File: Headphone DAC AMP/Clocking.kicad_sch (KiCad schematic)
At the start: 9 parts, among them Y1 LMK6CE049152CDLFR, Y2 LMK6CE049152CDLFR, Y3 ASDLJ-E-45.1584MHz

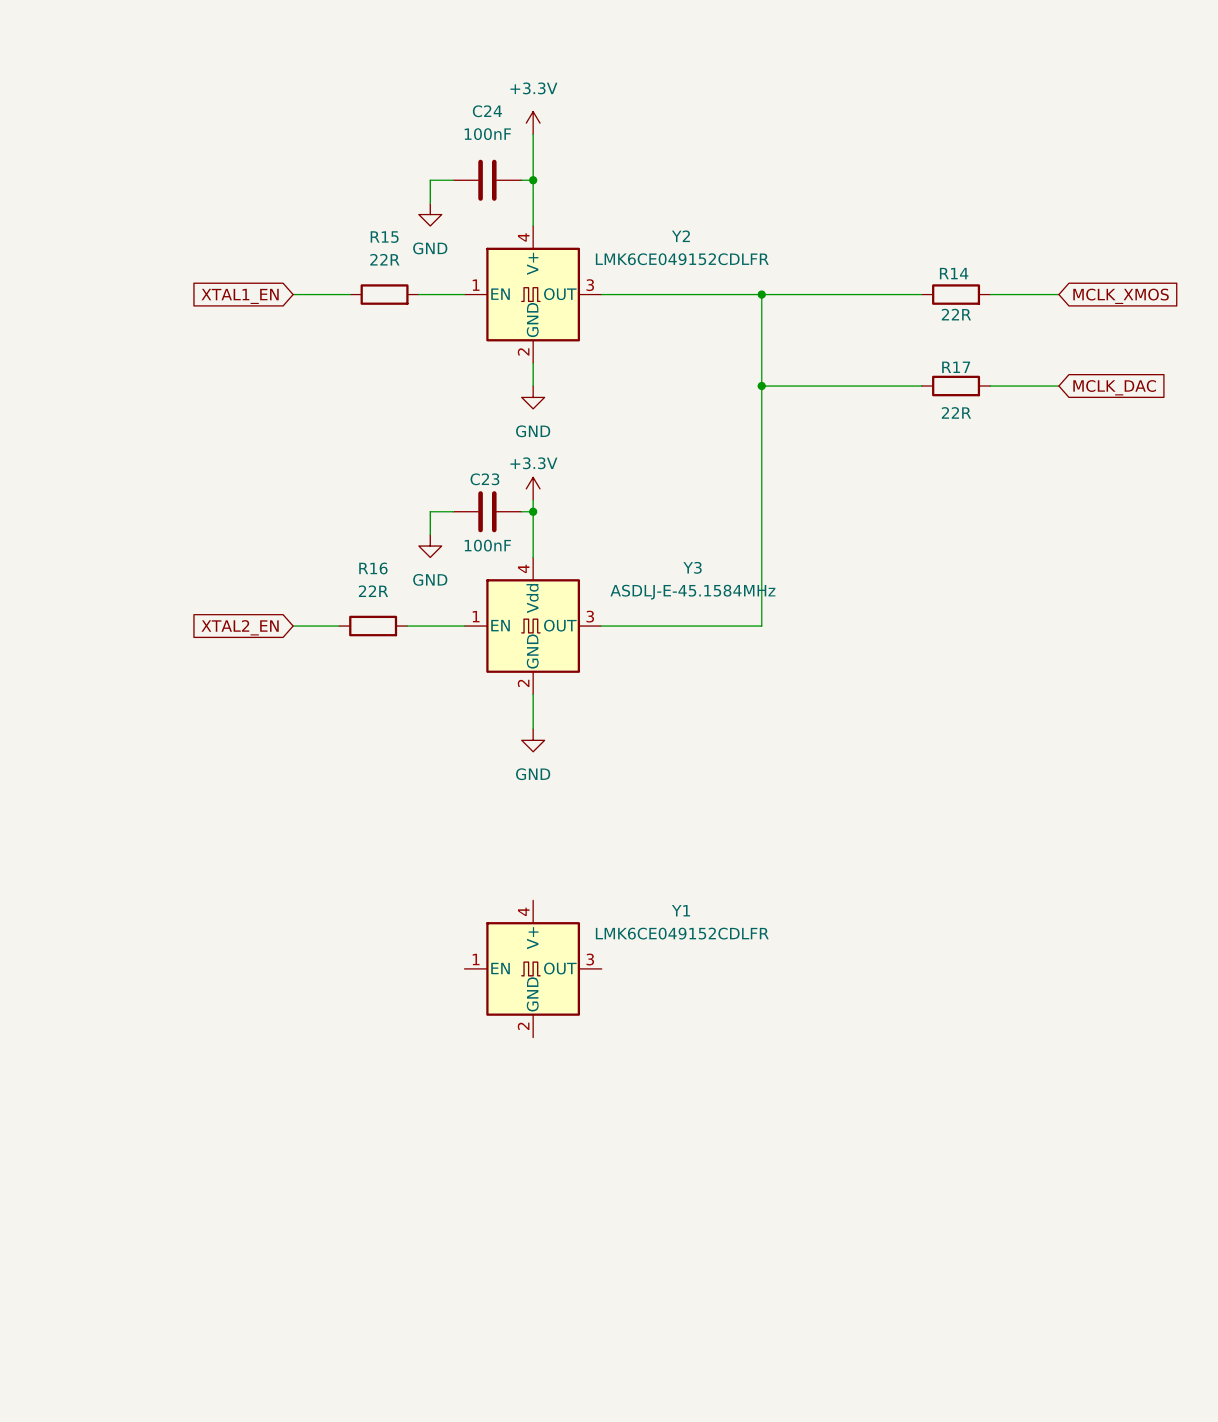
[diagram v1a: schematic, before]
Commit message: Completed a significant amount of the power and routing
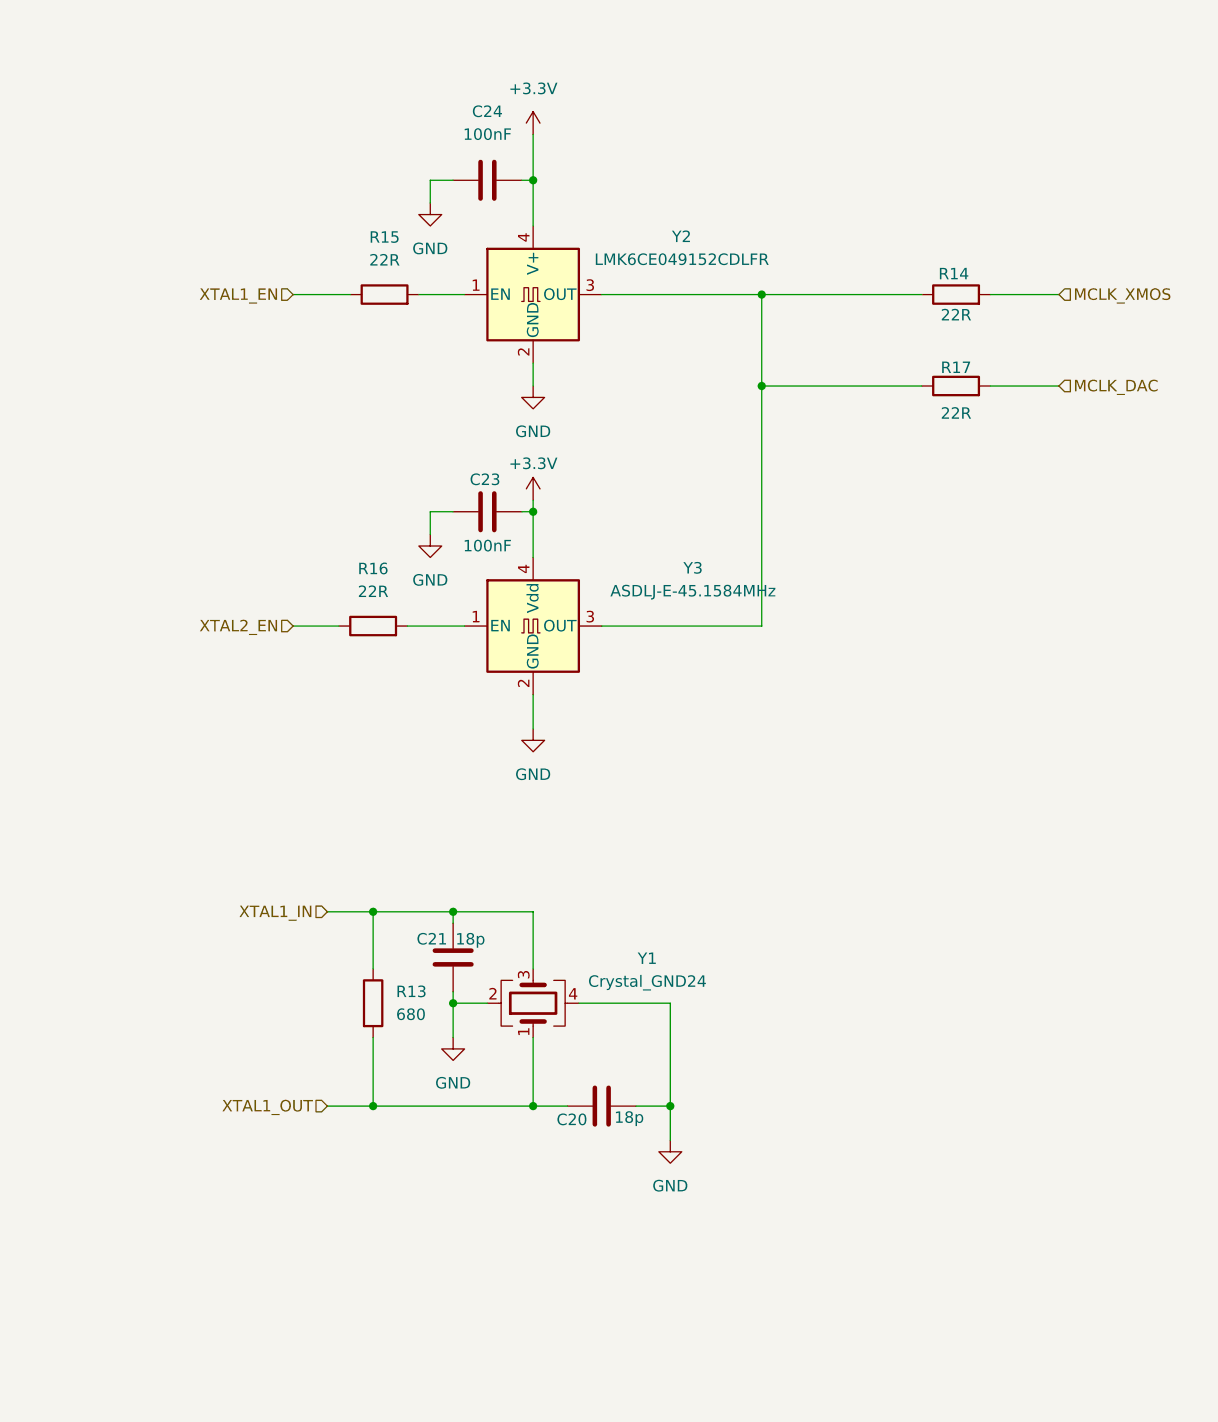
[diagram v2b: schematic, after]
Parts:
- removed Y1: LMK6CE049152CDLFR, Oscillator:Oscillator_SMD_EuroQuartz_XO32-4Pin_3.2x2.5mm, symbol Oscillator:XO32
- added C20, C21: 18p, Capacitor_SMD:C_0805_2012Metric_Pad1.18x1.45mm_HandSolder, symbol Device:C
- added R13: 680, Resistor_SMD:R_0805_2012Metric_Pad1.20x1.40mm_HandSolder, symbol Device:R
- added Y1: Crystal_GND24, Crystal:Crystal_SMD_3225-4Pin_3.2x2.5mm_HandSoldering, symbol Device:Crystal_GND24
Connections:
- net GND: now also C20.1, C21.2, Y1.2, Y1.4
- new net XTAL1_IN: C21.1, R13.1, Y1.3
- new net XTAL1_OUT: C20.2, R13.2, Y1.1

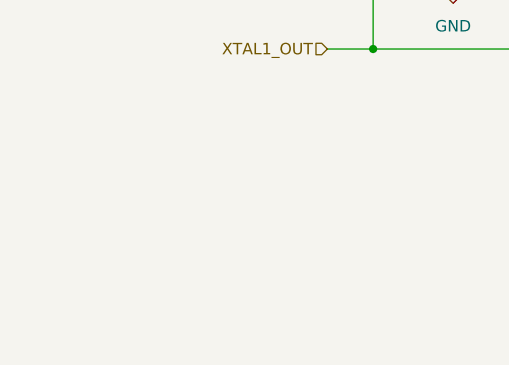
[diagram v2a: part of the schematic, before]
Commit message: Added ground and 0.9v
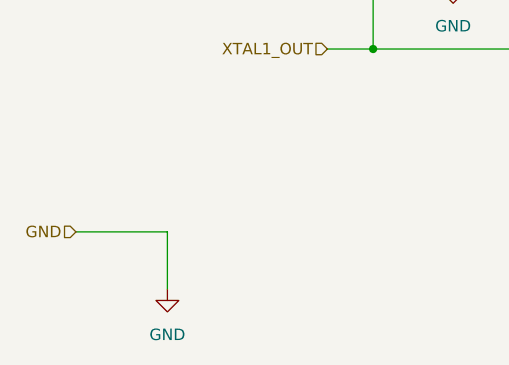
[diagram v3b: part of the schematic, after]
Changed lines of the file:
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@@
+	(wire
+		(pts
+			(xy 46.99 158.75) (xy 57.15 158.75)
+		)
+		(stroke
+			(width 0)
+			(type default)
+		)
+	)
 	(wire
 		(pts
@@
 		(pts
 			(xy 123.19 58.42) (xy 140.97 58.42)
+		)
+		(stroke
+			(width 0)
+			(type default)
+		)
+	)
+	(wire
+		(pts
+			(xy 57.15 158.75) (xy 57.15 165.1)
 		)
 		(stroke
@@
 			)
 			(justify left)
+		)
+	)
+	(hierarchical_label "GND"
+		(shape input)
+		(at 46.99 158.75 180)
+		(effects
+			(font
+				(size 1.27 1.27)
+			)
+			(justify right)
 		)
 	)
@@
 					(unit 1)
 				)
+			)
+		)
+	)
+	(symbol
+		(lib_id "power:GND")
+		(at 57.15 165.1 0)
+		(unit 1)
+		(exclude_from_sim no)
+		(in_bom yes)
+		(on_board yes)
+		(dnp no)
+		(fields_autoplaced yes)
+		(property "Reference" "#PWR083"
+			(at 57.15 171.45 0)
+			(effects
+				(font
+					(size 1.27 1.27)
+				)
+				(hide yes)
+			)
+		)
+		(property "Value" "GND"
+			(at 57.15 170.18 0)
+			(effects
+				(font
+					(size 1.27 1.27)
+				)
+			)
+		)
+		(property "Footprint" ""
+			(at 57.15 165.1 0)
+			(effects
+				(font
+					(size 1.27 1.27)
+				)
+				(hide yes)
+			)
+		)
+		(property "Datasheet" ""
+			(at 57.15 165.1 0)
+			(effects
+				(font
+					(size 1.27 1.27)
+				)
+				(hide yes)
+			)
+		)
+		(property "Description" "Power symbol creates a global label with name \"GND\" , ground"
+			(at 57.15 165.1 0)
+			(effects
+				(font
+					(size 1.27 1.27)
+				)
+				(hide yes)
+			)
+		)
+		(pin "1"
+		)
+		(instances
+			(project "Headphone DAC AMP"
+				(path "/d034eddd-efbc-47be-a25c-37cbfbab4cd8/e0b8fe34-d476-48aa-82d1-b0ba2e6c9788"
+					(reference "#PWR083")
+					(unit 1)
+				)

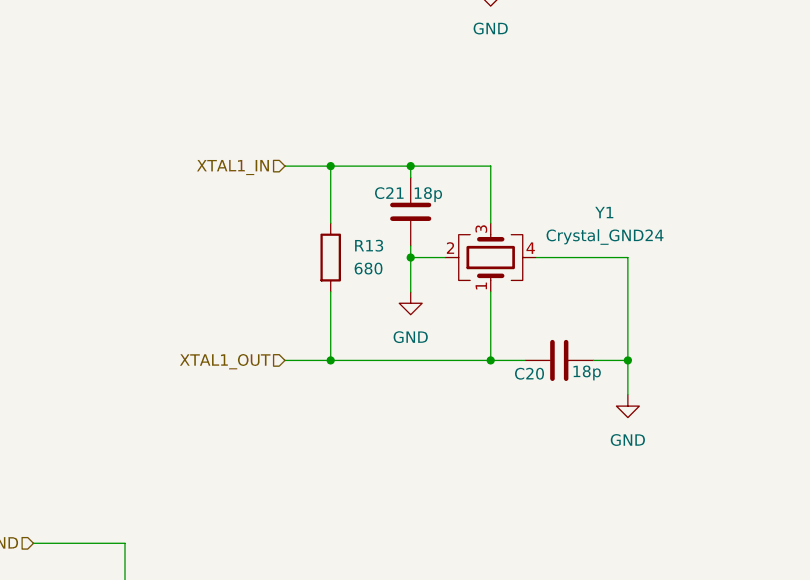
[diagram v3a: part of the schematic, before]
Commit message: fixed 24MHz clock and send draft 1 to tait
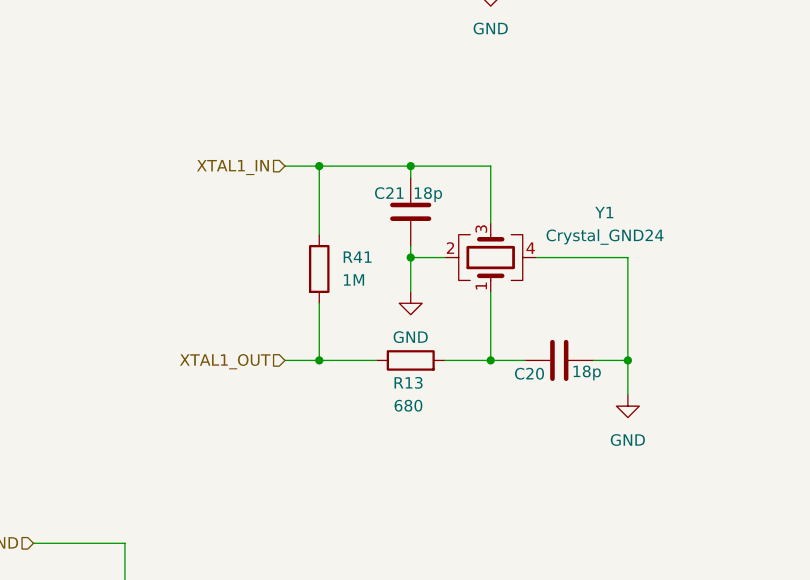
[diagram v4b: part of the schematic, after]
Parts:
- added R41: 1M, symbol Device:R
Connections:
- net XTAL1_IN: now also R41.1; no longer R13.1
- net XTAL1_OUT: now also R13.1, R41.2; no longer C20.2, R13.2, Y1.1
- new net: C20.2, R13.2, Y1.1
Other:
- moved on the sheet: R13
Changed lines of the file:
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@@
+	)
+	(junction
+		(at 97.79 138.43)
+		(diameter 0)
+		(color 0 0 0 0)
 	)
 	(junction
@@
 	)
 	(junction
-		(at 80.01 116.84)
-		(diameter 0)
-		(color 0 0 0 0)
-	)
-	(junction
-		(at 97.79 138.43)
+		(at 78.74 116.84)
 		(diameter 0)
 		(color 0 0 0 0)
@@
 	)
 	(junction
+		(at 78.74 138.43)
+		(diameter 0)
+		(color 0 0 0 0)
+	)
+	(junction
 		(at 97.79 72.39)
 		(diameter 0)
 		(color 0 0 0 0)
 	)
-	(junction
-		(at 80.01 138.43)
-		(diameter 0)
-		(color 0 0 0 0)
-	)
 	(wire
 		(pts
@@
 	(wire
 		(pts
-			(xy 74.93 116.84) (xy 80.01 116.84)
-		)
-		(stroke
-			(width 0)
-			(type default)
-		)
-	)
-	(wire
-		(pts
 			(xy 97.79 30.48) (xy 97.79 35.56)
 		)
@@
 	(wire
 		(pts
+			(xy 78.74 132.08) (xy 78.74 138.43)
+		)
+		(stroke
+			(width 0)
+			(type default)
+		)
+	)
+	(wire
+		(pts
+			(xy 78.74 116.84) (xy 88.9 116.84)
+		)
+		(stroke
+			(width 0)
+			(type default)
+		)
+	)
+	(wire
+		(pts
 			(xy 113.03 138.43) (xy 113.03 142.24)
 		)
@@
 	(wire
 		(pts
-			(xy 80.01 130.81) (xy 80.01 138.43)
-		)
-		(stroke
-			(width 0)
-			(type default)
-		)
-	)
-	(wire
-		(pts
 			(xy 88.9 116.84) (xy 97.79 116.84)
 		)
@@
 	(wire
 		(pts
-			(xy 80.01 116.84) (xy 80.01 123.19)
-		)
-		(stroke
-			(width 0)
-			(type default)
-		)
-	)
-	(wire
-		(pts
 			(xy 123.19 48.26) (xy 140.97 48.26)
 		)
@@
 	(wire
 		(pts
+			(xy 74.93 138.43) (xy 78.74 138.43)
+		)
+		(stroke
+			(width 0)
+			(type default)
+		)
+	)
+	(wire
+		(pts
 			(xy 105.41 85.09) (xy 123.19 85.09)
 		)
@@
 	(wire
 		(pts
-			(xy 101.6 138.43) (xy 97.79 138.43)
-		)
-		(stroke
-			(width 0)
-			(type default)
-		)
-	)
-	(wire
-		(pts
 			(xy 71.12 85.09) (xy 76.2 85.09)
 		)
@@
 	(wire
 		(pts
-			(xy 80.01 116.84) (xy 88.9 116.84)
+			(xy 74.93 116.84) (xy 78.74 116.84)
+		)
+		(stroke
+			(width 0)
+			(type default)
+		)
+	)
+	(wire
+		(pts
+			(xy 78.74 116.84) (xy 78.74 124.46)
 		)
 		(stroke
@@
 	(wire
 		(pts
-			(xy 80.01 138.43) (xy 74.93 138.43)
-		)
-		(stroke
-			(width 0)
-			(type default)
-		)
-	)
-	(wire
-		(pts
 			(xy 148.59 58.42) (xy 156.21 58.42)
 		)
@@
 	(wire
 		(pts
-			(xy 80.01 138.43) (xy 97.79 138.43)
+			(xy 78.74 138.43) (xy 85.09 138.43)
 		)
 		(stroke
@@
 	(wire
 		(pts
+			(xy 92.71 138.43) (xy 97.79 138.43)
+		)
+		(stroke
+			(width 0)
+			(type default)
+		)
+	)
+	(wire
+		(pts
 			(xy 97.79 71.12) (xy 97.79 72.39)
+		)
+		(stroke
+			(width 0)
+			(type default)
+		)
+	)
+	(wire
+		(pts
+			(xy 97.79 138.43) (xy 101.6 138.43)
 		)
 		(stroke
@@
 	(symbol
 		(lib_id "Device:R")
-		(at 80.01 127 0)
-		(unit 1)
-		(exclude_from_sim no)
-		(in_bom yes)
-		(on_board yes)
-		(dnp no)
-		(fields_autoplaced yes)
+		(at 88.9 138.43 90)
+		(unit 1)
+		(exclude_from_sim no)
+		(in_bom yes)
+		(on_board yes)
+		(dnp no)
 		(property "Reference" "R13"
-			(at 82.55 125.7299 0)
-			(effects
-				(font
-					(size 1.27 1.27)
-				)
-				(justify left)
+			(at 88.646 140.97 90)
+			(effects
+				(font
+					(size 1.27 1.27)
+				)
 			)
 		)
 		(property "Value" "680"
-			(at 82.55 128.2699 0)
-			(effects
-				(font
-					(size 1.27 1.27)
-				)
-				(justify left)
+			(at 88.646 143.51 90)
+			(effects
+				(font
+					(size 1.27 1.27)
+				)
 			)
 		)
 		(property "Footprint" "Resistor_SMD:R_0805_2012Metric_Pad1.20x1.40mm_HandSolder"
-			(at 78.232 127 90)
+			(at 88.9 140.208 90)
 			(effects
 				(font
@@
 		)
 		(property "Datasheet" "~"
-			(at 80.01 127 0)
+			(at 88.9 138.43 0)
 			(effects
 				(font
@@
 		)
 		(property "Description" "Resistor"
-			(at 80.01 127 0)
+			(at 88.9 138.43 0)
 			(effects
 				(font
@@
 					(unit 1)
 				)
+			)
+		)
+	)
+	(symbol
+		(lib_id "Device:R")
+		(at 78.74 128.27 0)
+		(unit 1)
+		(exclude_from_sim no)
+		(in_bom yes)
+		(on_board yes)
+		(dnp no)
+		(fields_autoplaced yes)
+		(property "Reference" "R41"
+			(at 81.28 126.9999 0)
+			(effects
+				(font
+					(size 1.27 1.27)
+				)
+				(justify left)
+			)
+		)
+		(property "Value" "1M"
+			(at 81.28 129.5399 0)
+			(effects
+				(font
+					(size 1.27 1.27)
+				)
+				(justify left)
+			)
+		)
+		(property "Footprint" ""
+			(at 76.962 128.27 90)
+			(effects
+				(font
+					(size 1.27 1.27)
+				)
+				(hide yes)
+			)
+		)
+		(property "Datasheet" "~"
+			(at 78.74 128.27 0)
+			(effects
+				(font
+					(size 1.27 1.27)
+				)
+				(hide yes)
+			)
+		)
+		(property "Description" "Resistor"
+			(at 78.74 128.27 0)
+			(effects
+				(font
+					(size 1.27 1.27)
+				)
+				(hide yes)
+			)
+		)
+		(pin "1"
+		)
+		(pin "2"
+		)
+		(instances
+			(project ""
+				(path "/d034eddd-efbc-47be-a25c-37cbfbab4cd8/e0b8fe34-d476-48aa-82d1-b0ba2e6c9788"
+					(reference "R41")
+					(unit 1)
+				)

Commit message: "fuck my chud life"
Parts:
- R41: footprint (none) -> Inductor_SMD:L_0805_2012Metric
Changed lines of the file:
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@@
 			)
 		)
-		(property "Footprint" ""
+		(property "Footprint" "Inductor_SMD:L_0805_2012Metric"
 			(at 76.962 128.27 90)
 			(effects

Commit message: uPDATED MORE FOOTPRINTS
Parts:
- C23, C24: value 100nF -> 100n; footprint Capacitor_SMD:C_0805_2012Metric_Pad1.18x1.45mm_HandSolder -> Capacitor_SMD:C_0402_1005Metric_Pad0.74x0.62mm_HandSolder
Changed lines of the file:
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@@
 			)
 		)
-		(property "Value" "100nF"
+		(property "Value" "100n"
 			(at 92.71 30.48 90)
 			(effects
@@
 			)
 		)
-		(property "Footprint" "Capacitor_SMD:C_0805_2012Metric_Pad1.18x1.45mm_HandSolder"
+		(property "Footprint" "Capacitor_SMD:C_0402_1005Metric_Pad0.74x0.62mm_HandSolder"
 			(at 88.9 36.5252 0)
 			(effects
@@
 			)
 		)
-		(property "Value" "100nF"
+		(property "Value" "100n"
 			(at 92.71 76.2 90)
 			(effects
@@
 			)
 		)
-		(property "Footprint" "Capacitor_SMD:C_0805_2012Metric_Pad1.18x1.45mm_HandSolder"
+		(property "Footprint" "Capacitor_SMD:C_0402_1005Metric_Pad0.74x0.62mm_HandSolder"
 			(at 88.9 73.3552 0)
 			(effects
